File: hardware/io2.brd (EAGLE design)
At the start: 98.1 x 60.3 mm, 42 parts, among them IC1 PCF8574T, IC2 74HC14D, IC3 74HC74D, Q1 BC857BSMD, Q2 BSS123, Q3 BSS123

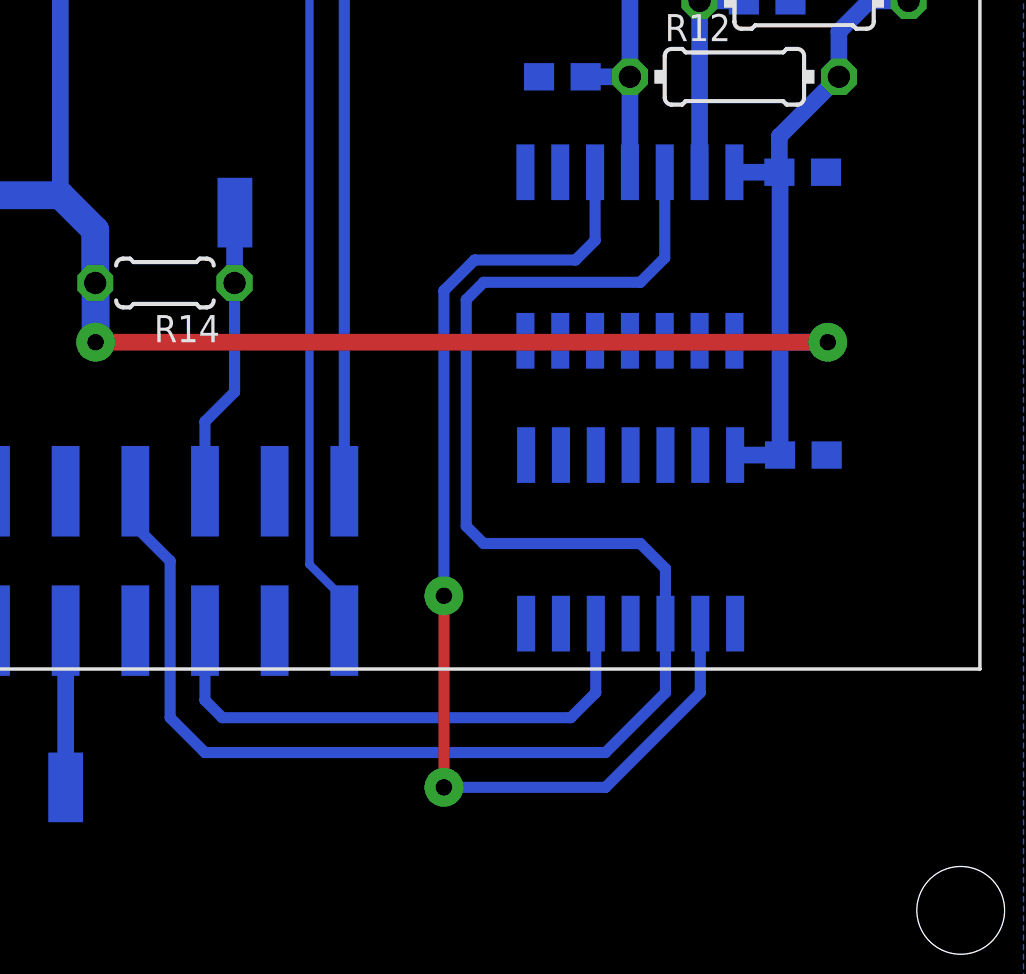
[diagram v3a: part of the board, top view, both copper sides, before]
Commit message: rotary encoder fixed
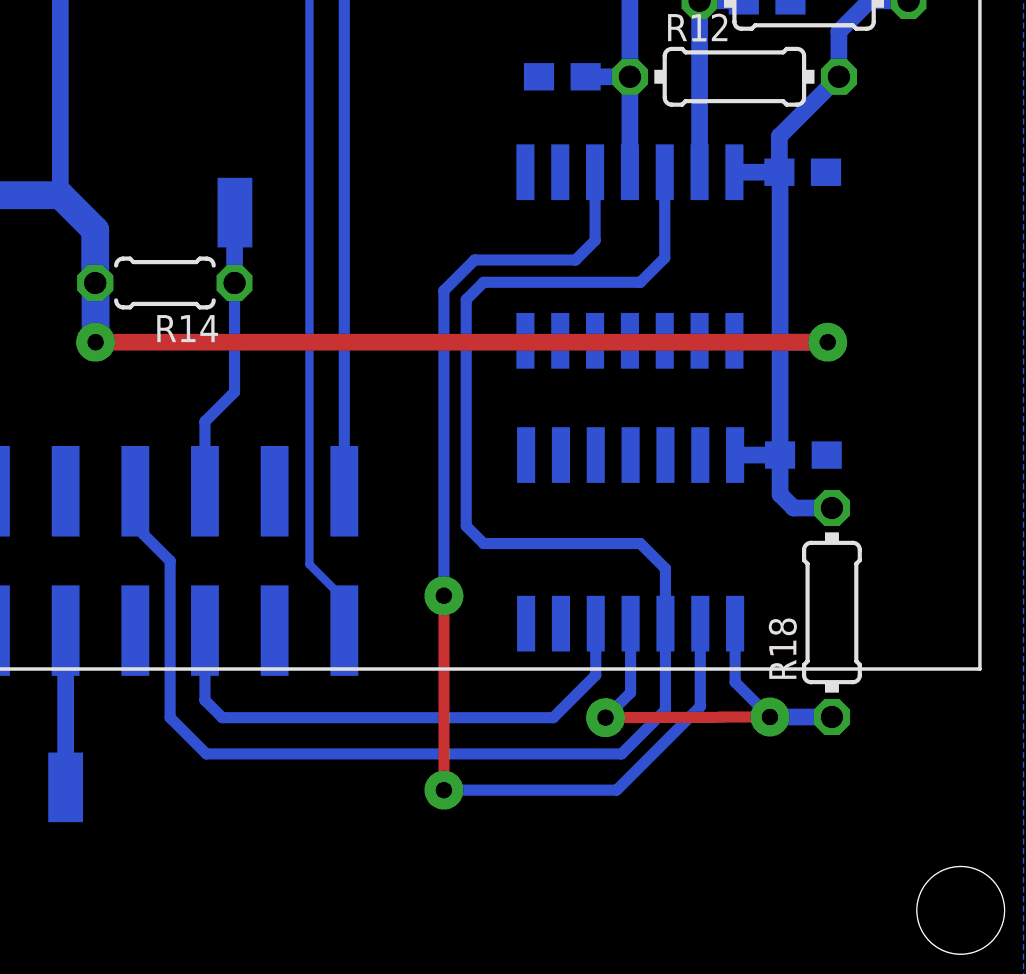
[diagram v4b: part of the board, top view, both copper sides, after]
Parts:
- added R18: (no value), rcl:0204/7
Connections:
- new net N$2: IC3.1, IC3.4, R18.1
- net 3V: now also R18.2
- net GND: no longer IC3.1, IC3.4
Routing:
- net N$2: track 0.00 -> 16.0 mm, vias 0 -> 2
- net 3V: track 134.3 -> 137.8 mm
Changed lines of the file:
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@@
 <element name="PAD1" library="wirepad" package="SMD1,27-2,54" value="" x="83.439" y="41.3004" rot="MR0"/>
 <element name="PAD8" library="wirepad" package="SMD1,27-2,54" value="" x="85.979" y="41.3004" rot="MR0"/>
+<element name="R18" library="rcl" package="0204/7" value="" x="90.805" y="13.3604" rot="R90"/>
 </elements>
 <signals>
@@
 <contactref element="C7" pad="2"/>
 <contactref element="IC3" pad="7"/>
-<contactref element="IC3" pad="4"/>
-<contactref element="IC3" pad="1"/>
 <contactref element="IC3" pad="10"/>
 <contactref element="IC3" pad="13"/>
@@
 <wire x1="87.2744" y1="19.1008" x2="88.9136" y2="19.1008" width="0.6096" layer="16"/>
 <wire x1="88.9136" y1="19.1008" x2="88.9136" y2="23.2156" width="0.6096" layer="16"/>
-<wire x1="88.9136" y1="23.495" x2="88.9136" y2="29.3878" width="0.6096" layer="16"/>
+<wire x1="88.9136" y1="23.2156" x2="88.9136" y2="29.3878" width="0.6096" layer="16"/>
 <wire x1="88.9136" y1="29.3878" x2="88.8882" y2="29.4132" width="0.6096" layer="16"/>
 <wire x1="88.8882" y1="29.4132" x2="87.249" y2="29.4132" width="0.6096" layer="16"/>
@@
 <wire x1="63.9572" y1="25.3619" x2="63.9445" y2="25.3746" width="1.016" layer="16"/>
 <wire x1="90.6526" y1="23.2156" x2="88.9136" y2="23.2156" width="0.6096" layer="16"/>
-<wire x1="88.9136" y1="23.2156" x2="88.9136" y2="23.495" width="0.6096" layer="16"/>
+<contactref element="R18" pad="2"/>
+<wire x1="88.9136" y1="19.1008" x2="88.9136" y2="17.6648" width="0.6096" layer="16"/>
+<wire x1="88.9136" y1="17.6648" x2="89.408" y2="17.1704" width="0.6096" layer="16"/>
+<wire x1="90.805" y1="17.1704" x2="89.408" y2="17.1704" width="0.6096" layer="16"/>
 </signal>
 <signal name="BACKLIGHT">
@@
 <contactref element="IC2" pad="12"/>
 <contactref element="IC3" pad="3"/>
-<wire x1="84.7344" y1="12.954" x2="84.7344" y2="10.4394" width="0.4064" layer="16"/>
+<wire x1="84.7344" y1="12.954" x2="84.7344" y2="9.8044" width="0.4064" layer="16"/>
 <contactref element="JP1" pad="8"/>
 <wire x1="65.405" y1="17.78" x2="65.405" y2="16.51" width="0.3048" layer="16"/>
 <wire x1="65.405" y1="16.51" x2="66.675" y2="15.24" width="0.4064" layer="16"/>
 <wire x1="66.675" y1="15.24" x2="66.675" y2="9.525" width="0.4064" layer="16"/>
-<wire x1="66.675" y1="9.525" x2="67.945" y2="8.255" width="0.4064" layer="16"/>
-<wire x1="67.945" y1="8.255" x2="82.55" y2="8.255" width="0.4064" layer="16"/>
-<wire x1="82.55" y1="8.255" x2="84.7344" y2="10.4394" width="0.4064" layer="16"/>
+<wire x1="66.675" y1="9.525" x2="67.9958" y2="8.2042" width="0.4064" layer="16"/>
 <wire x1="84.7344" y1="12.954" x2="84.7344" y2="14.9606" width="0.4064" layer="16"/>
 <wire x1="84.7344" y1="14.9606" x2="83.82" y2="15.875" width="0.4064" layer="16"/>
@@
 <wire x1="83.82" y1="25.4" x2="84.709" y2="26.289" width="0.4064" layer="16"/>
 <wire x1="84.709" y1="29.4132" x2="84.709" y2="26.289" width="0.4064" layer="16"/>
+<wire x1="84.7344" y1="9.8044" x2="83.1342" y2="8.2042" width="0.4064" layer="16"/>
+<wire x1="83.1342" y1="8.2042" x2="67.9958" y2="8.2042" width="0.4064" layer="16"/>
 </signal>
 <signal name="ROT_B_">
 <contactref element="IC2" pad="10"/>
 <contactref element="IC3" pad="2"/>
-<wire x1="86.0044" y1="12.954" x2="86.0044" y2="10.4394" width="0.4064" layer="16"/>
-<wire x1="86.0044" y1="10.4394" x2="82.55" y2="6.985" width="0.4064" layer="16"/>
-<wire x1="82.55" y1="6.985" x2="76.6572" y2="6.985" width="0.4064" layer="16"/>
-<via x="76.6572" y="6.985" extent="1-16" drill="0.6" diameter="1.4224" shape="octagon"/>
-<wire x1="76.6572" y1="6.985" x2="76.6572" y2="13.97" width="0.4064" layer="1"/>
+<via x="76.6572" y="6.8834" extent="1-16" drill="0.6" diameter="1.4224" shape="octagon"/>
+<wire x1="76.6572" y1="6.8834" x2="76.6572" y2="13.97" width="0.4064" layer="1"/>
 <via x="76.6572" y="13.97" extent="1-16" drill="0.6" diameter="1.4224" shape="octagon"/>
 <wire x1="81.4578" y1="26.2128" x2="82.169" y2="26.924" width="0.4064" layer="16"/>
@@
 <wire x1="76.6572" y1="25.0952" x2="77.7748" y2="26.2128" width="0.4064" layer="16"/>
 <wire x1="77.7748" y1="26.2128" x2="81.4578" y2="26.2128" width="0.4064" layer="16"/>
+<wire x1="76.6572" y1="6.8834" x2="82.9564" y2="6.8834" width="0.4064" layer="16"/>
+<wire x1="82.9564" y1="6.8834" x2="86.0044" y2="9.9314" width="0.4064" layer="16"/>
+<wire x1="86.0044" y1="12.954" x2="86.0044" y2="9.9314" width="0.4064" layer="16"/>
 </signal>
 <signal name="N$5">
@@
 <wire x1="67.945" y1="12.7" x2="67.945" y2="10.16" width="0.4064" layer="16"/>
 <wire x1="67.945" y1="10.16" x2="68.58" y2="9.525" width="0.4064" layer="16"/>
-<wire x1="68.58" y1="9.525" x2="81.28" y2="9.525" width="0.4064" layer="16"/>
-<wire x1="81.28" y1="9.525" x2="82.1944" y2="10.4394" width="0.4064" layer="16"/>
-<wire x1="82.1944" y1="12.954" x2="82.1944" y2="10.4394" width="0.4064" layer="16"/>
+<wire x1="68.58" y1="9.525" x2="80.645" y2="9.525" width="0.4064" layer="16"/>
+<wire x1="80.645" y1="9.525" x2="82.1944" y2="11.0744" width="0.4064" layer="16"/>
+<wire x1="82.1944" y1="12.954" x2="82.1944" y2="11.0744" width="0.4064" layer="16"/>
+</signal>
+<signal name="N$2">
+<contactref element="IC3" pad="4"/>
+<contactref element="IC3" pad="1"/>
+<wire x1="83.4644" y1="12.954" x2="83.4644" y2="10.4394" width="0.4064" layer="16"/>
+<wire x1="83.4644" y1="10.4394" x2="82.55" y2="9.525" width="0.4064" layer="16"/>
+<via x="82.55" y="9.525" extent="1-16" drill="0.6" diameter="1.4224" shape="octagon"/>
+<wire x1="82.55" y1="9.525" x2="88.5444" y2="9.5504" width="0.4064" layer="1"/>
+<via x="88.5444" y="9.5504" extent="1-16" drill="0.6" diameter="1.4224" shape="octagon"/>
+<wire x1="87.2744" y1="12.954" x2="87.2744" y2="10.8204" width="0.4064" layer="16"/>
+<wire x1="87.2744" y1="10.8204" x2="88.5444" y2="9.5504" width="0.4064" layer="16"/>
+<contactref element="R18" pad="1"/>
+<wire x1="88.5444" y1="9.5504" x2="90.805" y2="9.5504" width="0.6096" layer="16"/>
 </signal>
 </signals>
